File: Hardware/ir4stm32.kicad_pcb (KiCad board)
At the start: 2 copper layers, 81 x 52 mm, 76 parts, among them P1 + - R T, Q1 SS8050, Q2 SS8050, Q3 SS8050, Q4 SS8050, Q5 SS8050, Q6 SS8050, Q7 SS8050, Q8 SS8050, U1 XC6206P332MR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

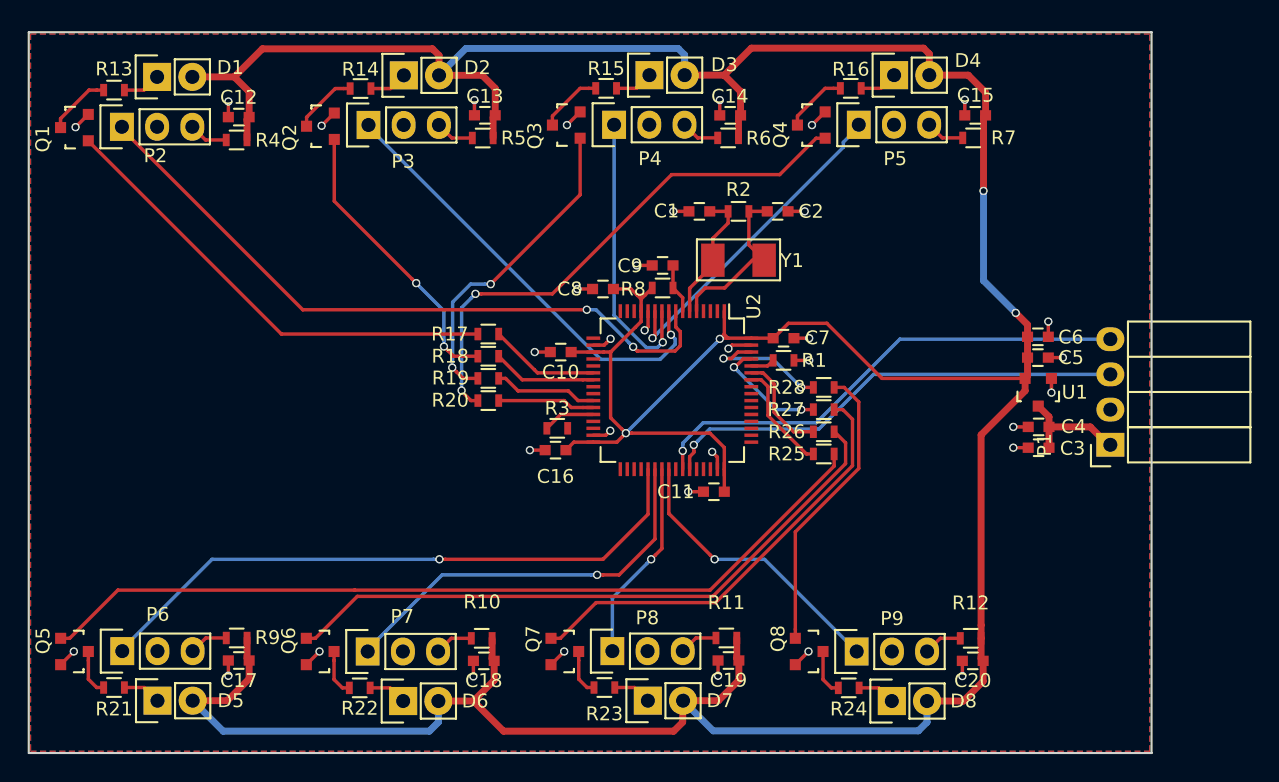
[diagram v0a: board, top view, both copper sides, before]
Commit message: fix: BOOT Options error
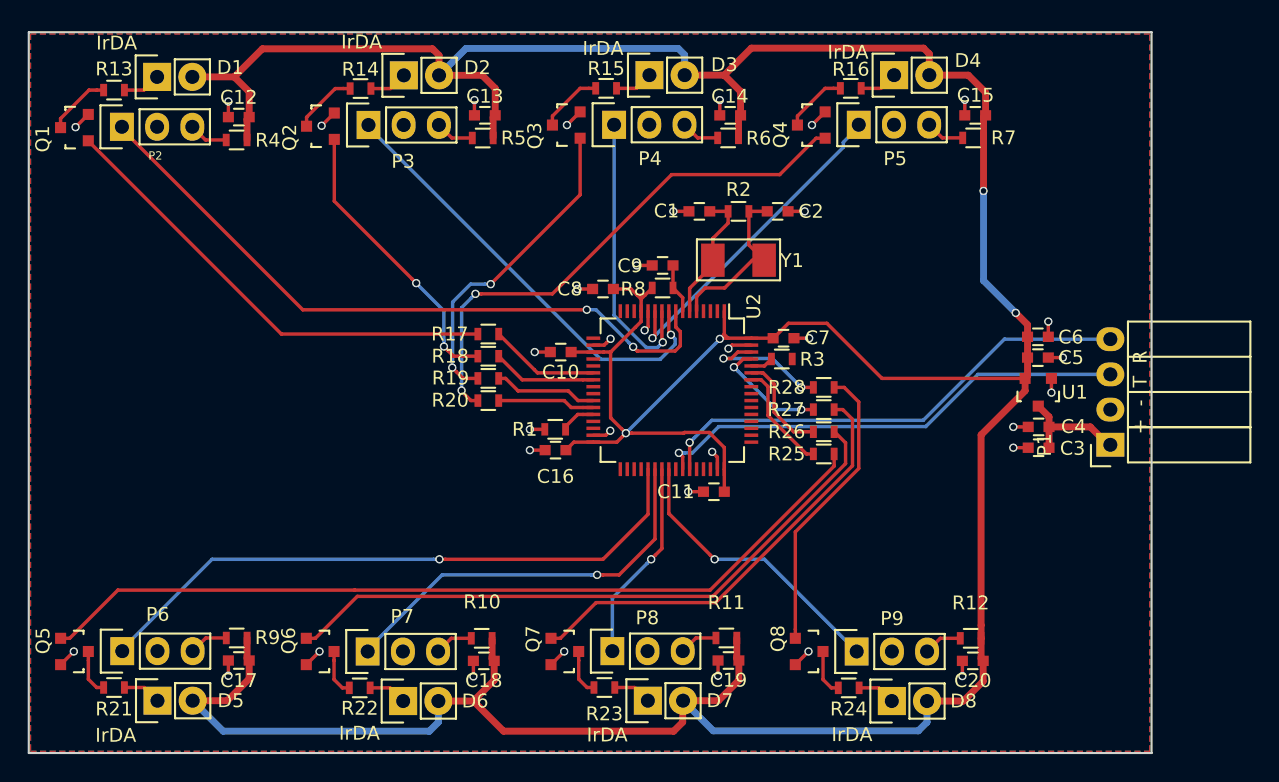
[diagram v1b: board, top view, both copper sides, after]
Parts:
- D1: value IrDA_CH1 -> IrDA
- D2: value IrDA_CH2 -> IrDA
- D3: value IrDA_CH3 -> IrDA
- D4: value IrDA_CH4 -> IrDA
- D5: value IrDA_CH5 -> IrDA
- D6: value IrDA_CH6 -> IrDA
- D7: value IrDA_CH7 -> IrDA
- D8: value IrDA_CH8 -> IrDA
- P1: value + - R T -> + - T R
- P2, P3, P4, P5, P6, P7, P8, P9: value (none) -> CONN_01X03
- Q1, Q2, Q3, Q4, Q5, Q6, Q7, Q8: value SS8050 -> Q_NPN_BEC
- Y1: value X50328MSD2GC -> 8MHz
- moved R1 17.2 mm to (152.0, 113.7), turned to 0 degrees
- moved R3 17.0 mm to (168.3, 108.6)
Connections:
- P1 pad 3: RX1 -> TX1
- P1 pad 4: TX1 -> RX1
- R1 pad 2: BOOT0 -> BOOT1
- R3 pad 1: Net-(R3-Pad1) -> (no net)
- R3 pad 2: BOOT1 -> BOOT0
- U2 pad 14: Net-(U2-Pad14) -> (no net)
- U2 pad 15: Net-(U2-Pad15) -> (no net)
- U2 pad 16: Net-(U2-Pad16) -> (no net)
- U2 pad 17: Net-(U2-Pad17) -> (no net)
- U2 pad 2: Net-(U2-Pad2) -> (no net)
- U2 pad 20: Net-(U2-Pad20) -> (no net)
- U2 pad 21: Net-(U2-Pad21) -> (no net)
- U2 pad 24: Net-(U2-Pad24) -> (no net)
- U2 pad 25: Net-(U2-Pad25) -> (no net)
- U2 pad 29: Net-(U2-Pad29) -> (no net)
- U2 pad 3: Net-(U2-Pad3) -> (no net)
- U2 pad 30: Net-(U2-Pad30) -> (no net)
- U2 pad 33: Net-(U2-Pad33) -> (no net)
- U2 pad 34: Net-(U2-Pad34) -> (no net)
- U2 pad 35: Net-(U2-Pad35) -> (no net)
- U2 pad 36: Net-(U2-Pad36) -> (no net)
- U2 pad 4: Net-(U2-Pad4) -> (no net)
- U2 pad 41: Net-(U2-Pad41) -> (no net)
- U2 pad 44: Net-(U2-Pad44) -> (no net)
- U2 pad 45: Net-(U2-Pad45) -> (no net)
- U2 pad 46: Net-(U2-Pad46) -> (no net)
- U2 pad 49: Net-(U2-Pad49) -> (no net)
- U2 pad 50: Net-(U2-Pad50) -> (no net)
- U2 pad 51: Net-(U2-Pad51) -> (no net)
- U2 pad 52: Net-(U2-Pad52) -> (no net)
- U2 pad 53: Net-(U2-Pad53) -> (no net)
- U2 pad 54: Net-(U2-Pad54) -> (no net)
- U2 pad 55: Net-(U2-Pad55) -> (no net)
- U2 pad 56: Net-(U2-Pad56) -> (no net)
- U2 pad 57: Net-(U2-Pad57) -> (no net)
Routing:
- net RX1: track 34.0 -> 35.4 mm
- net BOOT1: track 3.76 -> 2.56 mm
- net TX1: track 35.8 -> 34.8 mm
